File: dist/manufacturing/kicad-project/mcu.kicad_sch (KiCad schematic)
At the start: 22 parts, among them SW1 SW1, U16 STM32G0B1CBT6, U17 W25Q32JVSSIQ, Y1 Y1

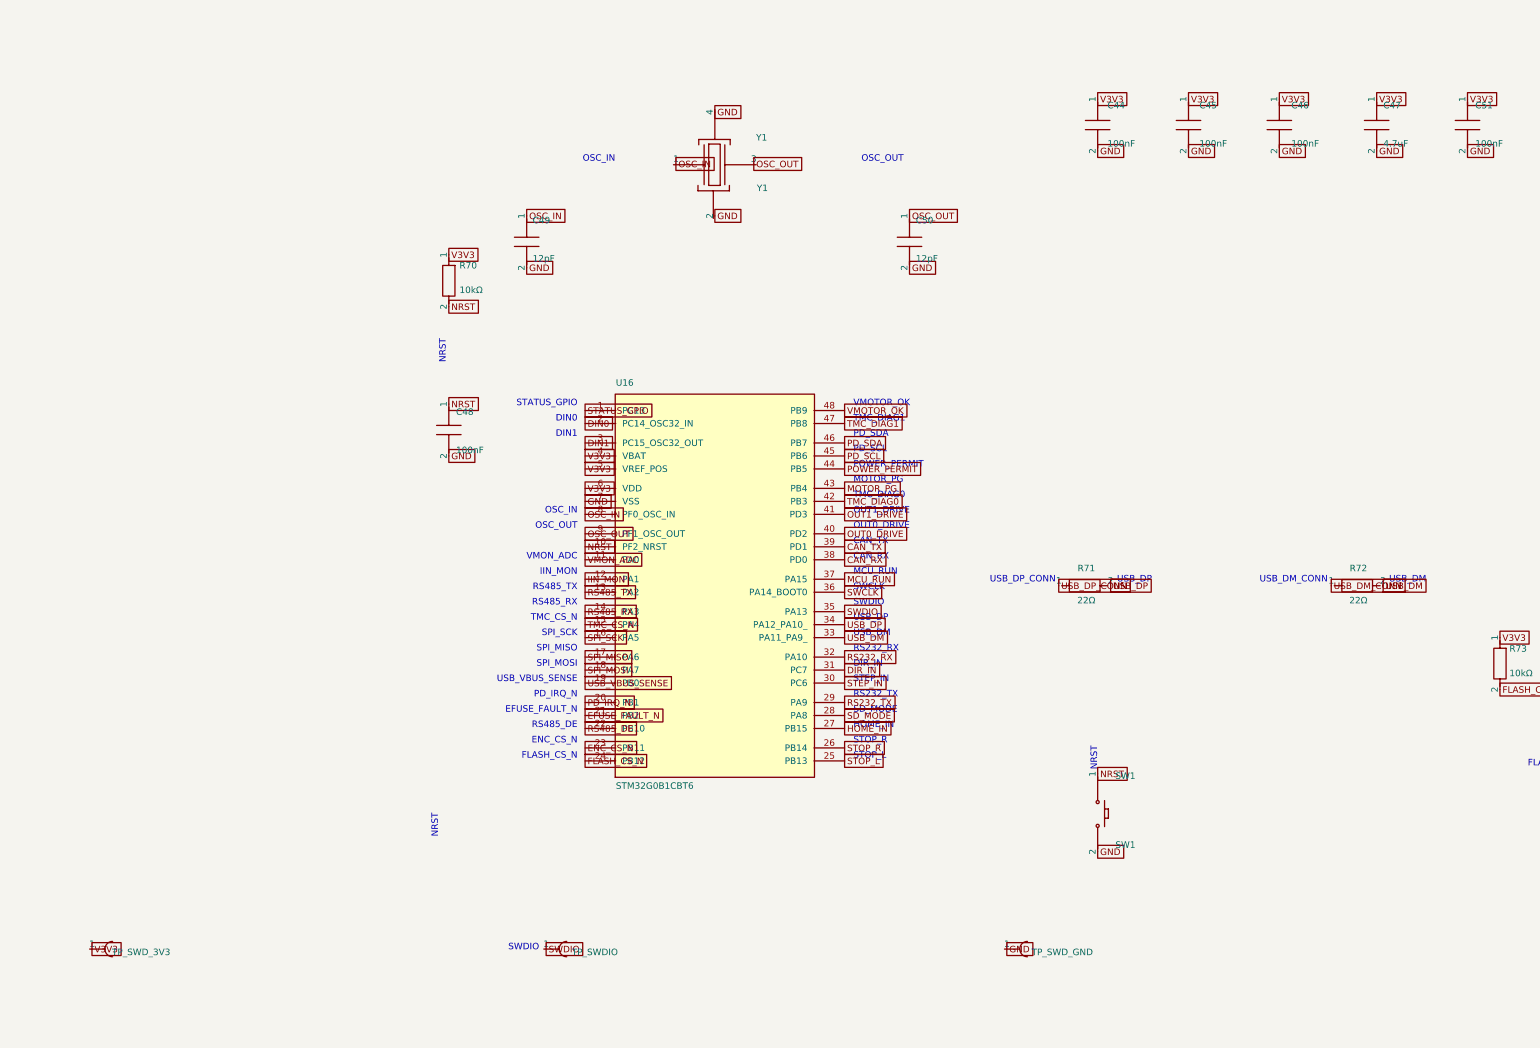
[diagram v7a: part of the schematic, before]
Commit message: Complete top-side routing and verify reference-board ECO
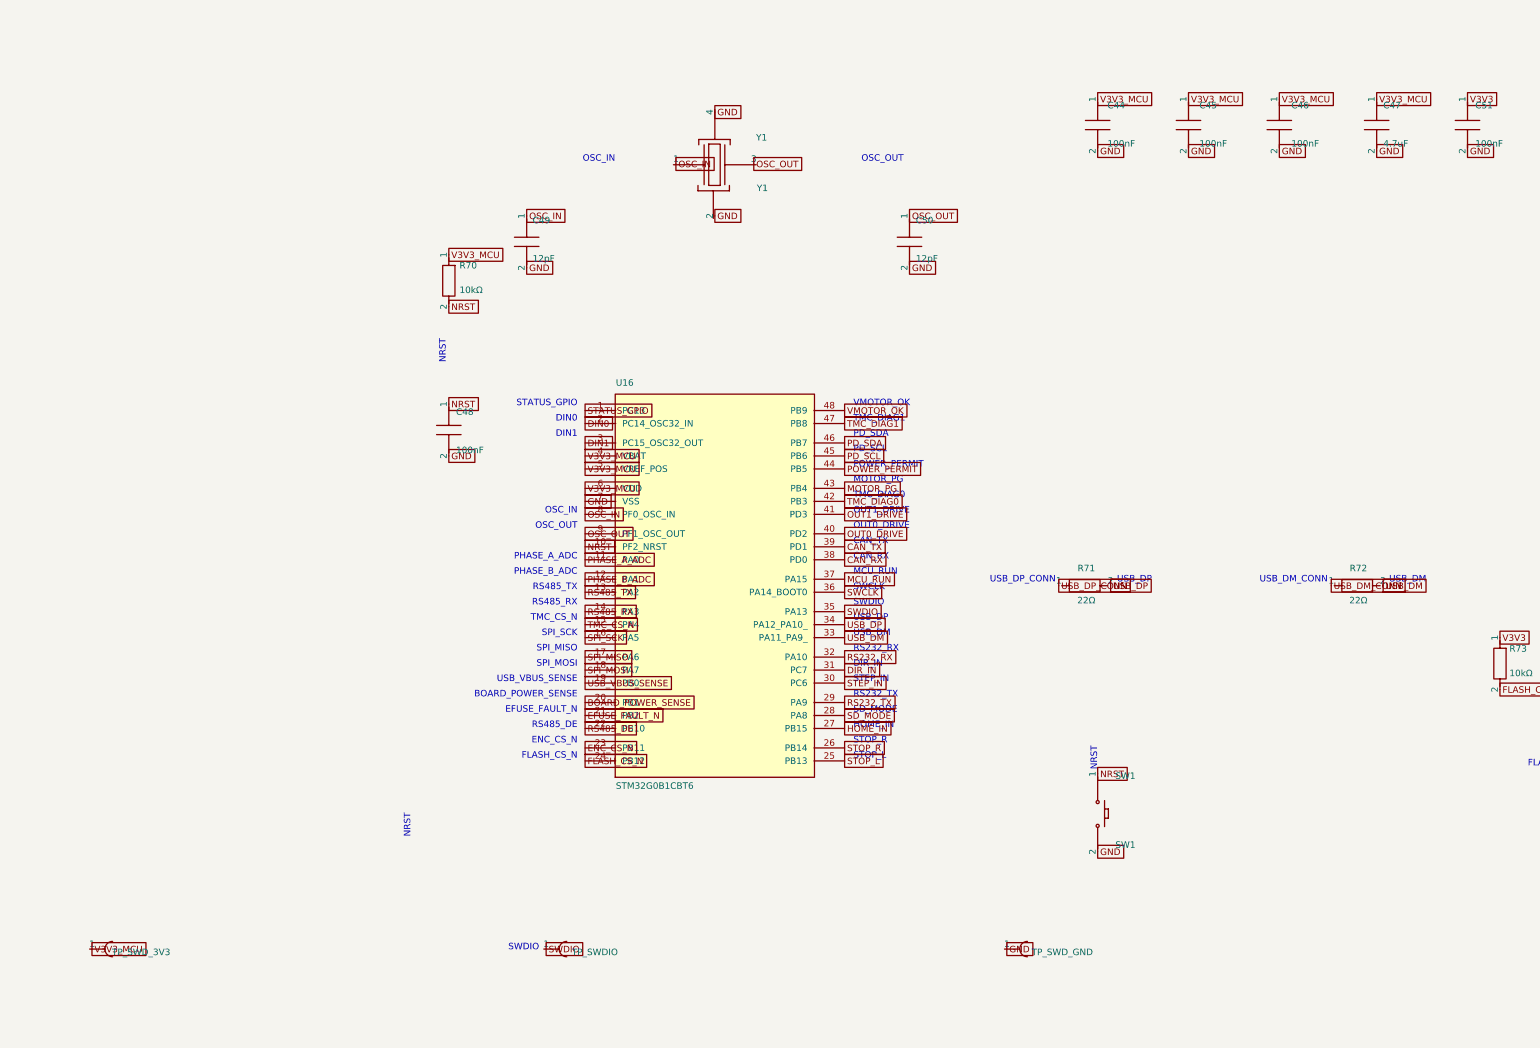
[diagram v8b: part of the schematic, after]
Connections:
- net V3V3: no longer C44.1, C45.1, C46.1, C47.1, R70.1, TP_SWD_3V3.1, U16.4 (VBAT), U16.5 (VREF_POS), U16.6 (VDD)
- net IIN_MON renamed PHASE_B_ADC
- net PD_IRQ_N renamed BOARD_POWER_SENSE
- net VMON_ADC renamed PHASE_A_ADC
- new net V3V3_MCU: C44.1, C45.1, C46.1, C47.1, R70.1, TP_SWD_3V3.1, U16.4 (VBAT), U16.5 (VREF_POS), U16.6 (VDD)
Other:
- note added: "BOARD_POWER_SENSE"
- note added: "PHASE_A_ADC"
- note added: "PHASE_B_ADC"
- note removed: "IIN_MON"
- note removed: "PD_IRQ_N"
- note removed: "VMON_ADC"
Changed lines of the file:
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@@
     (instances
       (project ""
-        (path "/4ef2daa1-40fc-426a-abb2-c834ba40a3c9/8831e43b-0a87-49bf-affb-c27877fcb531"
+        (path "/953e0ace-4c89-4879-a4e2-9aa73ffc3208/e4427830-eee7-4c40-931e-5cc1a87ac68b"
           (reference "U16")
           (unit 1)
@@
     (instances
       (project ""
-        (path "/4ef2daa1-40fc-426a-abb2-c834ba40a3c9/8831e43b-0a87-49bf-affb-c27877fcb531"
+        (path "/953e0ace-4c89-4879-a4e2-9aa73ffc3208/e4427830-eee7-4c40-931e-5cc1a87ac68b"
           (reference "C44")
           (unit 1)
@@
     (instances
       (project ""
-        (path "/4ef2daa1-40fc-426a-abb2-c834ba40a3c9/8831e43b-0a87-49bf-affb-c27877fcb531"
+        (path "/953e0ace-4c89-4879-a4e2-9aa73ffc3208/e4427830-eee7-4c40-931e-5cc1a87ac68b"
           (reference "C45")
           (unit 1)
@@
     (instances
       (project ""
-        (path "/4ef2daa1-40fc-426a-abb2-c834ba40a3c9/8831e43b-0a87-49bf-affb-c27877fcb531"
+        (path "/953e0ace-4c89-4879-a4e2-9aa73ffc3208/e4427830-eee7-4c40-931e-5cc1a87ac68b"
           (reference "C46")
           (unit 1)
@@
     (instances
       (project ""
-        (path "/4ef2daa1-40fc-426a-abb2-c834ba40a3c9/8831e43b-0a87-49bf-affb-c27877fcb531"
+        (path "/953e0ace-4c89-4879-a4e2-9aa73ffc3208/e4427830-eee7-4c40-931e-5cc1a87ac68b"
           (reference "C47")
           (unit 1)
@@
     (instances
       (project ""
-        (path "/4ef2daa1-40fc-426a-abb2-c834ba40a3c9/8831e43b-0a87-49bf-affb-c27877fcb531"
+        (path "/953e0ace-4c89-4879-a4e2-9aa73ffc3208/e4427830-eee7-4c40-931e-5cc1a87ac68b"
           (reference "R70")
           (unit 1)
@@
     (instances
       (project ""
-        (path "/4ef2daa1-40fc-426a-abb2-c834ba40a3c9/8831e43b-0a87-49bf-affb-c27877fcb531"
+        (path "/953e0ace-4c89-4879-a4e2-9aa73ffc3208/e4427830-eee7-4c40-931e-5cc1a87ac68b"
           (reference "C48")
           (unit 1)
@@
     (instances
       (project ""
-        (path "/4ef2daa1-40fc-426a-abb2-c834ba40a3c9/8831e43b-0a87-49bf-affb-c27877fcb531"
+        (path "/953e0ace-4c89-4879-a4e2-9aa73ffc3208/e4427830-eee7-4c40-931e-5cc1a87ac68b"
           (reference "R71")
           (unit 1)
@@
     (instances
       (project ""
-        (path "/4ef2daa1-40fc-426a-abb2-c834ba40a3c9/8831e43b-0a87-49bf-affb-c27877fcb531"
+        (path "/953e0ace-4c89-4879-a4e2-9aa73ffc3208/e4427830-eee7-4c40-931e-5cc1a87ac68b"
           (reference "R72")
           (unit 1)
@@
     (instances
       (project ""
-        (path "/4ef2daa1-40fc-426a-abb2-c834ba40a3c9/8831e43b-0a87-49bf-affb-c27877fcb531"
+        (path "/953e0ace-4c89-4879-a4e2-9aa73ffc3208/e4427830-eee7-4c40-931e-5cc1a87ac68b"
           (reference "Y1")
           (unit 1)
@@
     (instances
       (project ""
-        (path "/4ef2daa1-40fc-426a-abb2-c834ba40a3c9/8831e43b-0a87-49bf-affb-c27877fcb531"
+        (path "/953e0ace-4c89-4879-a4e2-9aa73ffc3208/e4427830-eee7-4c40-931e-5cc1a87ac68b"
           (reference "C49")
           (unit 1)
@@
     (instances
       (project ""
-        (path "/4ef2daa1-40fc-426a-abb2-c834ba40a3c9/8831e43b-0a87-49bf-affb-c27877fcb531"
+        (path "/953e0ace-4c89-4879-a4e2-9aa73ffc3208/e4427830-eee7-4c40-931e-5cc1a87ac68b"
           (reference "C50")
           (unit 1)
@@
     (instances
       (project ""
-        (path "/4ef2daa1-40fc-426a-abb2-c834ba40a3c9/8831e43b-0a87-49bf-affb-c27877fcb531"
+        (path "/953e0ace-4c89-4879-a4e2-9aa73ffc3208/e4427830-eee7-4c40-931e-5cc1a87ac68b"
           (reference "SW1")
           (unit 1)
@@
     (instances
       (project ""
-        (path "/4ef2daa1-40fc-426a-abb2-c834ba40a3c9/8831e43b-0a87-49bf-affb-c27877fcb531"
+        (path "/953e0ace-4c89-4879-a4e2-9aa73ffc3208/e4427830-eee7-4c40-931e-5cc1a87ac68b"
           (reference "TP_SWD_3V3")
           (unit 1)
@@
     (instances
       (project ""
-        (path "/4ef2daa1-40fc-426a-abb2-c834ba40a3c9/8831e43b-0a87-49bf-affb-c27877fcb531"
+        (path "/953e0ace-4c89-4879-a4e2-9aa73ffc3208/e4427830-eee7-4c40-931e-5cc1a87ac68b"
           (reference "TP_SWDIO")
           (unit 1)
@@
     (instances
       (project ""
-        (path "/4ef2daa1-40fc-426a-abb2-c834ba40a3c9/8831e43b-0a87-49bf-affb-c27877fcb531"
+        (path "/953e0ace-4c89-4879-a4e2-9aa73ffc3208/e4427830-eee7-4c40-931e-5cc1a87ac68b"
           (reference "TP_SWD_GND")
           (unit 1)
@@
     (instances
       (project ""
-        (path "/4ef2daa1-40fc-426a-abb2-c834ba40a3c9/8831e43b-0a87-49bf-affb-c27877fcb531"
+        (path "/953e0ace-4c89-4879-a4e2-9aa73ffc3208/e4427830-eee7-4c40-931e-5cc1a87ac68b"
           (reference "TP_SWCLK")
           (unit 1)
@@
     (instances
       (project ""
-        (path "/4ef2daa1-40fc-426a-abb2-c834ba40a3c9/8831e43b-0a87-49bf-affb-c27877fcb531"
+        (path "/953e0ace-4c89-4879-a4e2-9aa73ffc3208/e4427830-eee7-4c40-931e-5cc1a87ac68b"
           (reference "TP_NRST")
           (unit 1)
@@
     (instances
       (project ""
-        (path "/4ef2daa1-40fc-426a-abb2-c834ba40a3c9/8831e43b-0a87-49bf-affb-c27877fcb531"
+        (path "/953e0ace-4c89-4879-a4e2-9aa73ffc3208/e4427830-eee7-4c40-931e-5cc1a87ac68b"
           (reference "TP_STATUS")
           (unit 1)
@@
     (instances
       (project ""
-        (path "/4ef2daa1-40fc-426a-abb2-c834ba40a3c9/8831e43b-0a87-49bf-affb-c27877fcb531"
+        (path "/953e0ace-4c89-4879-a4e2-9aa73ffc3208/e4427830-eee7-4c40-931e-5cc1a87ac68b"
           (reference "U17")
           (unit 1)
@@
     (instances
       (project ""
-        (path "/4ef2daa1-40fc-426a-abb2-c834ba40a3c9/8831e43b-0a87-49bf-affb-c27877fcb531"
+        (path "/953e0ace-4c89-4879-a4e2-9aa73ffc3208/e4427830-eee7-4c40-931e-5cc1a87ac68b"
           (reference "R73")
           (unit 1)
@@
     (instances
       (project ""
-        (path "/4ef2daa1-40fc-426a-abb2-c834ba40a3c9/8831e43b-0a87-49bf-affb-c27877fcb531"
+        (path "/953e0ace-4c89-4879-a4e2-9aa73ffc3208/e4427830-eee7-4c40-931e-5cc1a87ac68b"
           (reference "C51")
           (unit 1)
@@
   )
   (text "NRST"
-    (at 107.76000000000002 191.74999999999997 -90)
+    (at 102.36000000000001 191.74999999999997 -90)
     (effects
       (font
@@
     )
   )
-  (text "VMON_ADC"
+  (text "PHASE_A_ADC"
     (at 135.675 139.09999999999997 0)
     (effects
@@
     )
   )
-  (text "IIN_MON"
+  (text "PHASE_B_ADC"
     (at 135.675 142.09999999999997 0)
     (effects
@@
     )
   )
-  (text "PD_IRQ_N"
+  (text "BOARD_POWER_SENSE"
     (at 135.675 166.09999999999997 0)
     (effects
@@
     (fields_autoplaced no)
   )
-  (global_label "V3V3"
+  (global_label "V3V3_MCU"
     (shape passive)
     (at 137.16 119.38 0)
@@
     (fields_autoplaced no)
   )
-  (global_label "V3V3"
+  (global_label "V3V3_MCU"
     (shape passive)
     (at 137.16 121.92 0)
@@
     (fields_autoplaced no)
   )
-  (global_label "V3V3"
+  (global_label "V3V3_MCU"
     (shape passive)
     (at 137.16 125.73 0)
@@
     (fields_autoplaced no)
   )
-  (global_label "VMON_ADC"
+  (global_label "PHASE_A_ADC"
     (shape passive)
     (at 137.16 139.7 0)
@@
     (fields_autoplaced no)
   )
-  (global_label "IIN_MON"
+  (global_label "PHASE_B_ADC"
     (shape passive)
     (at 137.16 143.51 0)
@@
     (fields_autoplaced no)
   )
-  (global_label "PD_IRQ_N"
+  (global_label "BOARD_POWER_SENSE"
     (shape passive)
     (at 137.16 167.64 0)
@@
     (fields_autoplaced no)
   )
-  (global_label "V3V3"
+  (global_label "V3V3_MCU"
     (shape passive)
     (at 237.49 49.53 0)
@@
     (fields_autoplaced no)
   )
-  (global_label "V3V3"
+  (global_label "V3V3_MCU"
     (shape passive)
     (at 255.27 49.53 0)
@@
     (fields_autoplaced no)
   )
-  (global_label "V3V3"
+  (global_label "V3V3_MCU"
     (shape passive)
     (at 273.05 49.53 0)
@@
     (fields_autoplaced no)
   )
-  (global_label "V3V3"
+  (global_label "V3V3_MCU"
     (shape passive)
     (at 292.1 49.53 0)
@@
     (fields_autoplaced no)
   )
-  (global_label "V3V3"
+  (global_label "V3V3_MCU"
     (shape passive)
     (at 110.49 80.01 0)
@@
     (fields_autoplaced no)
   )
-  (global_label "V3V3"
+  (global_label "V3V3_MCU"
     (shape passive)
     (at 40.64 215.9 0)
